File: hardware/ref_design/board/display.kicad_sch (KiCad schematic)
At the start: 29 parts, among them J3 FH12-50S-0.5SH(55), Q5 AO3400A, Q6 AO3400A, U6 MCP6002

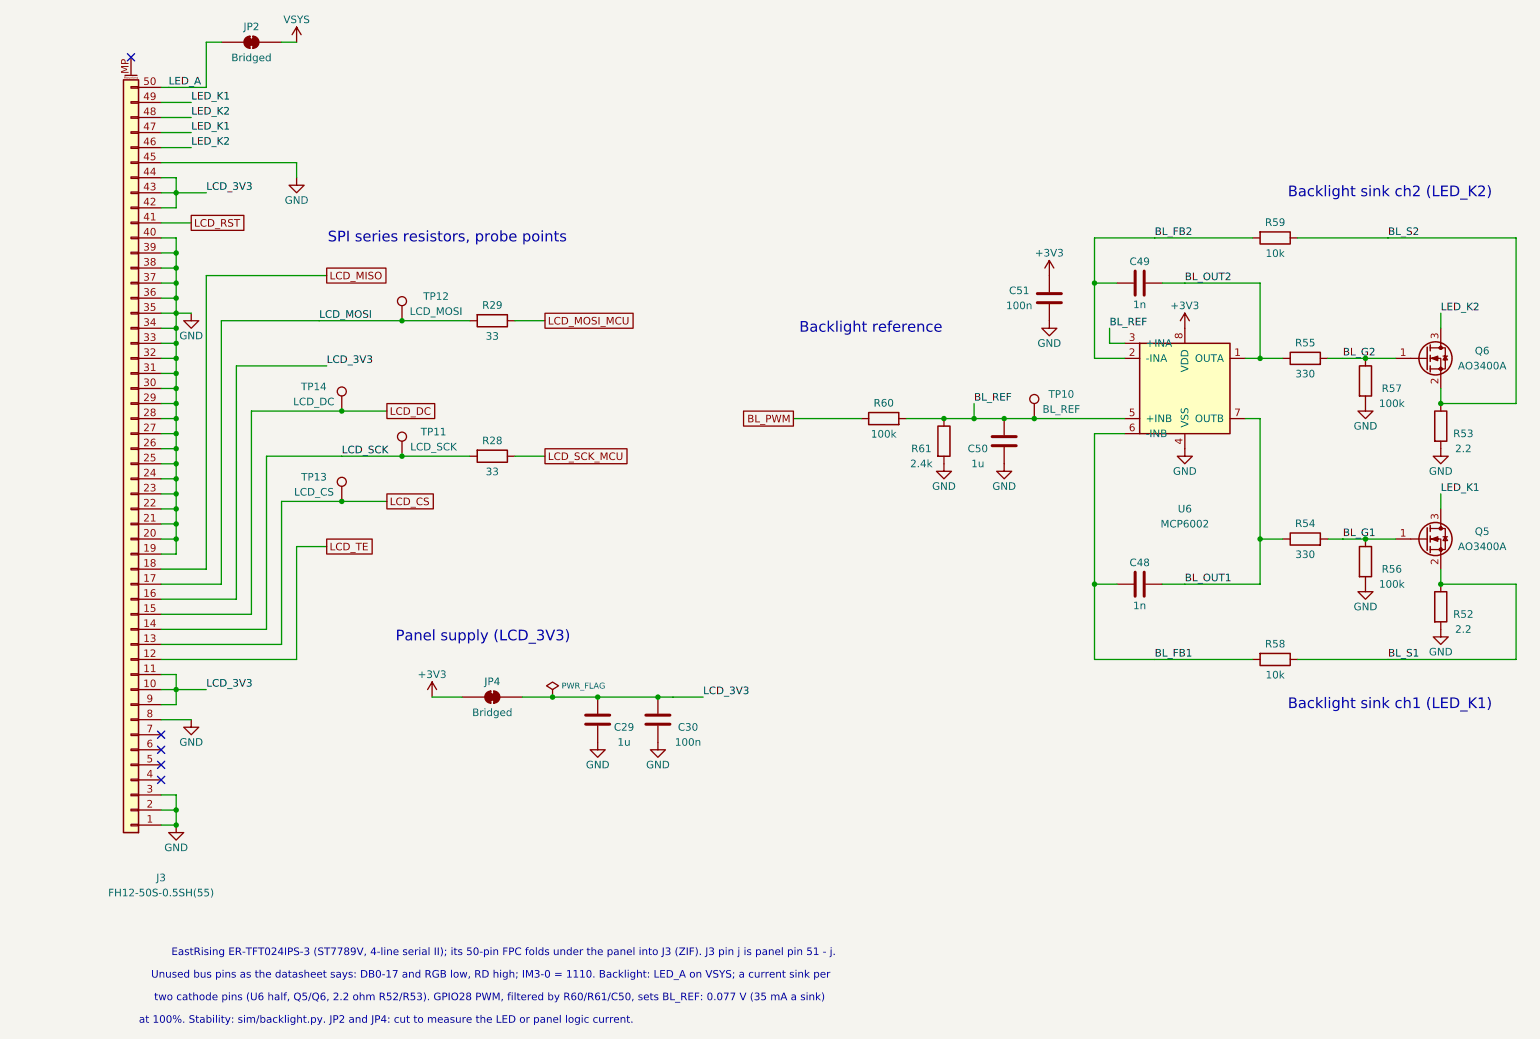
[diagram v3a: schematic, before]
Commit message: ref_design: schematic regenerated for the ER-TFT035IPS-6 (ERC 0, netlist and pin review pass)
Co-Authored-By: Claude Sonnet 5.5 <noreply@anthropic.com>
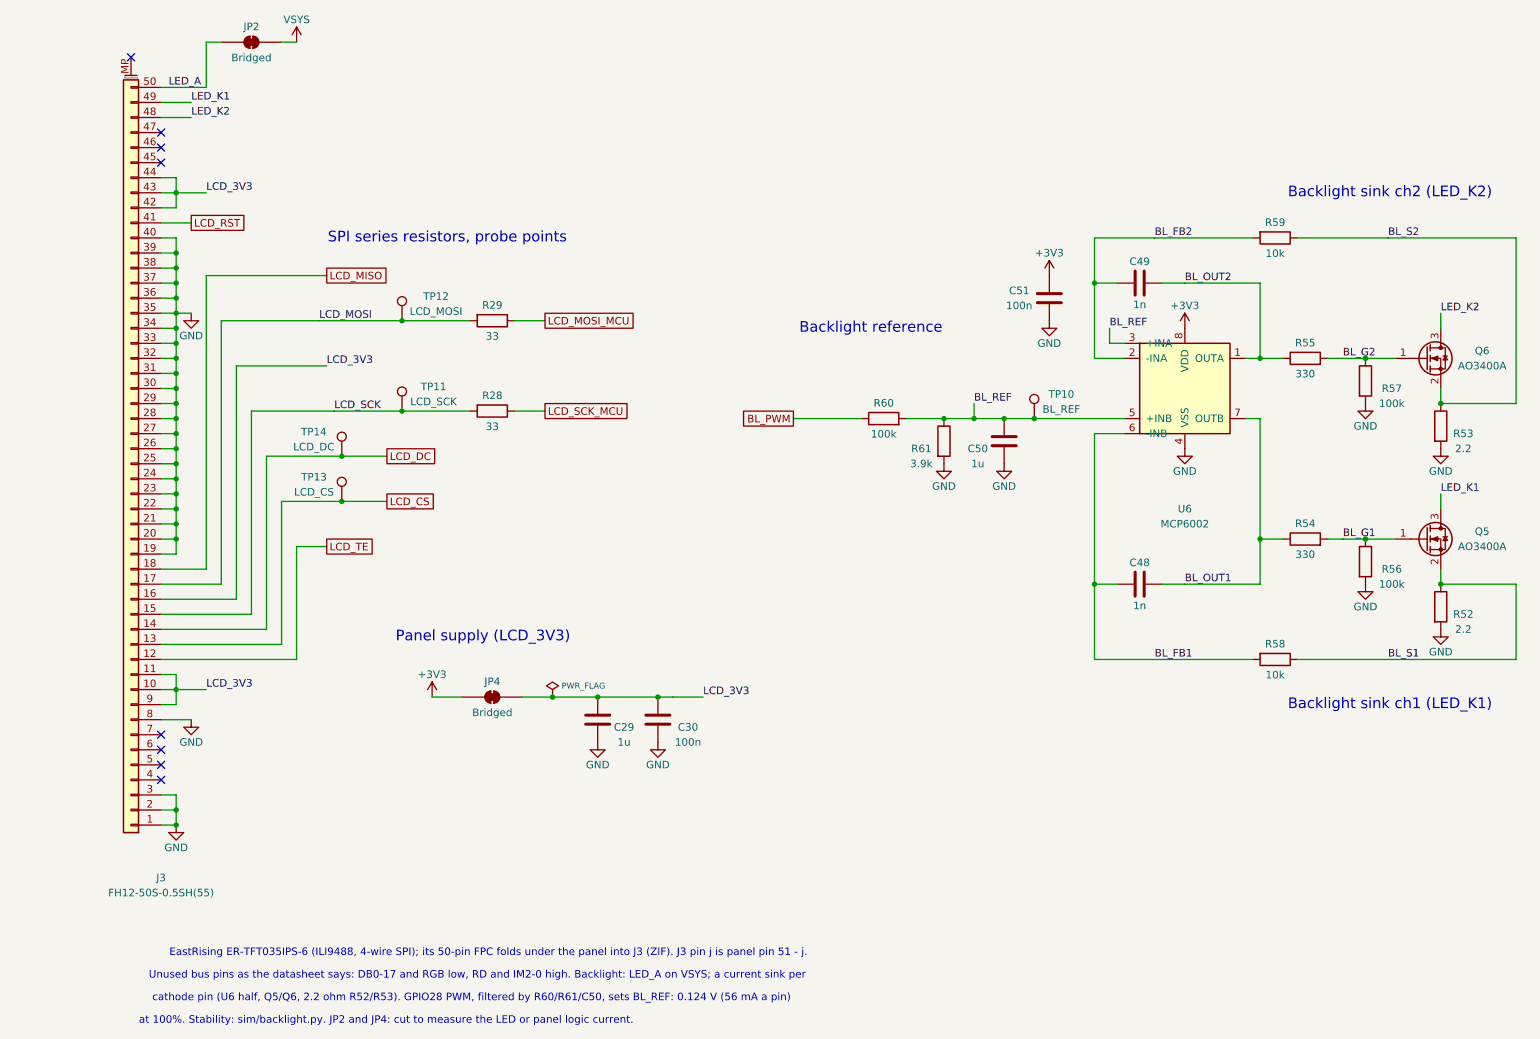
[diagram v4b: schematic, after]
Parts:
- R61: value 2.4k -> 3.9k; LCSC C25882 -> C51721; MPN 0402WGF2401TCE -> 0402WGF3901TCE
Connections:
- net GND: no longer J3.45 (Pin_45)
- net LCD_DC: now also J3.14 (Pin_14); no longer J3.15 (Pin_15)
- net LCD_SCK: now also J3.15 (Pin_15); no longer J3.14 (Pin_14)
- net LED_K1: no longer J3.47 (Pin_47)
- net LED_K2: no longer J3.46 (Pin_46)
- no-connect marks 5 -> 8
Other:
- note added: "EastRising ER-TFT035IPS-6 (ILI9488, 4-wire SPI); its 50-pin FPC folds under the panel into J3 (ZIF). J3 pin j is panel pin 51 - j."
- note added: "Unused bus pins as the datasheet says: DB0-17 and RGB low, RD and IM2-0 high. Backlight: LED_A on VSYS; a current sink per"
- note added: "cathode pin (U6 half, Q5/Q6, 2.2 ohm R52/R53). GPIO28 PWM, filtered by R60/R61/C50, sets BL_REF: 0.124 V (56 mA a pin)"
- note removed: "EastRising ER-TFT024IPS-3 (ST7789V, 4-line serial II); its 50-pin FPC folds under the panel into J3 (ZIF). J3 pin j is panel pin 51 - j."
- note removed: "Unused bus pins as the datasheet says: DB0-17 and RGB low, RD high; IM3-0 = 1110. Backlight: LED_A on VSYS; a current sink per"
- note removed: "two cathode pins (U6 half, Q5/Q6, 2.2 ohm R52/R53). GPIO28 PWM, filtered by R60/R61/C50, sets BL_REF: 0.077 V (35 mA a sink)"
- moved on the sheet: R28, TP11, TP14

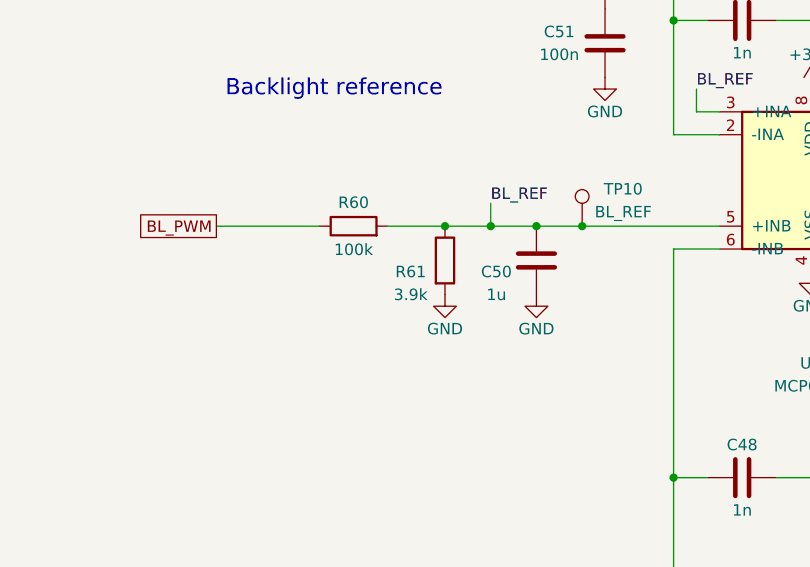
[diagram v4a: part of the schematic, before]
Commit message: ref_design V&V round 3, schematic: R61 3.74k (DEC-31), R14 47k and R43 220k with no clamp (DEC-17), RN1-RN4 47k (DEC-24), U10 buffer on VBAT_SENSE, 10k B4460 NTC for TH1, J4 JST SH, pin reviews
Co-Authored-By: Claude Sonnet 5.5 <noreply@anthropic.com>
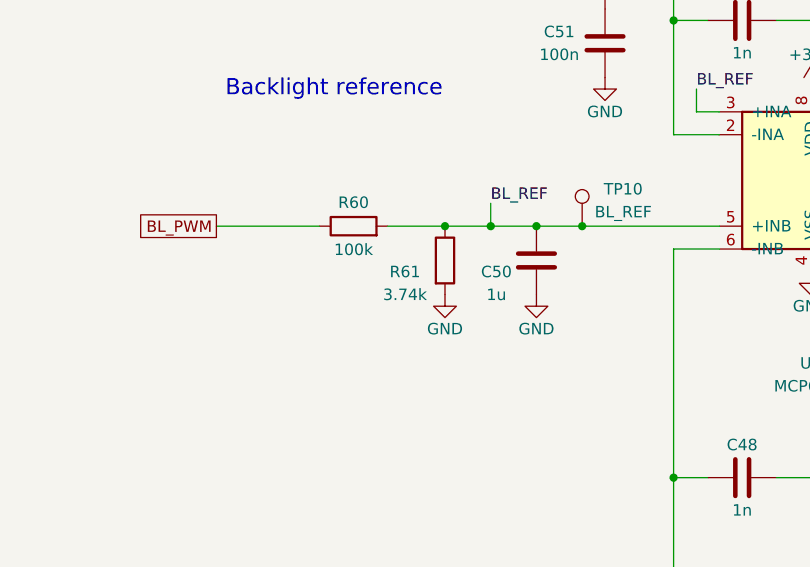
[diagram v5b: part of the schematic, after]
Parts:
- R61: value 3.9k -> 3.74k; LCSC C51721 -> C15172; MPN 0402WGF3901TCE -> 0402WGF3741TCE
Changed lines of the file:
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@@
 		(dnp no)
 		(property "Reference" "R61"
-			(at 156.21 90.17 0)
-			(show_name no)
-			(do_not_autoplace no)
-			(effects
-				(font
-					(size 1.27 1.27)
-				)
-			)
-		)
-		(property "Value" "3.9k"
-			(at 156.21 92.71 0)
+			(at 155.575 90.17 0)
+			(show_name no)
+			(do_not_autoplace no)
+			(effects
+				(font
+					(size 1.27 1.27)
+				)
+			)
+		)
+		(property "Value" "3.74k"
+			(at 155.575 92.71 0)
 			(show_name no)
 			(do_not_autoplace no)
@@
 			)
 		)
-		(property "LCSC" "C51721"
+		(property "LCSC" "C15172"
 			(at 160.02 88.9 0)
 			(hide yes)
@@
 			)
 		)
-		(property "MPN" "0402WGF3901TCE"
+		(property "MPN" "0402WGF3741TCE"
 			(at 160.02 88.9 0)
 			(hide yes)
@@
 		(in_pos_files yes)
 		(dnp no)
-		(property "Reference" "#PWR076"
+		(property "Reference" "#PWR080"
 			(at 50.8 21.59 0)
 			(hide yes)
@@
 			(project "battler"
 				(path "/8922e0a8-6f76-52f6-b0ec-4de6a784796f/99b2b9c1-5178-5fd9-a3fe-39987bd8b040"
-					(reference "#PWR076")
+					(reference "#PWR080")
 					(unit 1)
 				)
@@
 		(in_pos_files yes)
 		(dnp no)
-		(property "Reference" "#PWR077"
+		(property "Reference" "#PWR081"
 			(at 33.02 67.31 0)
 			(hide yes)
@@
 			(project "battler"
 				(path "/8922e0a8-6f76-52f6-b0ec-4de6a784796f/99b2b9c1-5178-5fd9-a3fe-39987bd8b040"
-					(reference "#PWR077")
+					(reference "#PWR081")
 					(unit 1)
 				)
@@
 		(in_pos_files yes)
 		(dnp no)
-		(property "Reference" "#PWR078"
+		(property "Reference" "#PWR082"
 			(at 33.02 135.89 0)
 			(hide yes)
@@
 			(project "battler"
 				(path "/8922e0a8-6f76-52f6-b0ec-4de6a784796f/99b2b9c1-5178-5fd9-a3fe-39987bd8b040"
-					(reference "#PWR078")
+					(reference "#PWR082")
 					(unit 1)
 				)
@@
 		(in_pos_files yes)
 		(dnp no)
-		(property "Reference" "#PWR079"
+		(property "Reference" "#PWR083"
 			(at 30.48 153.67 0)
 			(hide yes)
@@
 			(project "battler"
 				(path "/8922e0a8-6f76-52f6-b0ec-4de6a784796f/99b2b9c1-5178-5fd9-a3fe-39987bd8b040"
-					(reference "#PWR079")
+					(reference "#PWR083")
 					(unit 1)
 				)
@@
 		(in_pos_files yes)
 		(dnp no)
-		(property "Reference" "#PWR080"
+		(property "Reference" "#PWR084"
 			(at 73.66 132.08 0)
 			(hide yes)
@@
 			(project "battler"
 				(path "/8922e0a8-6f76-52f6-b0ec-4de6a784796f/99b2b9c1-5178-5fd9-a3fe-39987bd8b040"
-					(reference "#PWR080")
+					(reference "#PWR084")
 					(unit 1)
 				)
@@
 		(in_pos_files yes)
 		(dnp no)
-		(property "Reference" "#PWR081"
+		(property "Reference" "#PWR085"
 			(at 101.6 139.7 0)
 			(hide yes)
@@
 			(project "battler"
 				(path "/8922e0a8-6f76-52f6-b0ec-4de6a784796f/99b2b9c1-5178-5fd9-a3fe-39987bd8b040"
-					(reference "#PWR081")
+					(reference "#PWR085")
 					(unit 1)
 				)
@@
 		(in_pos_files yes)
 		(dnp no)
-		(property "Reference" "#PWR082"
+		(property "Reference" "#PWR086"
 			(at 111.76 139.7 0)
 			(hide yes)
@@
 			(project "battler"
 				(path "/8922e0a8-6f76-52f6-b0ec-4de6a784796f/99b2b9c1-5178-5fd9-a3fe-39987bd8b040"
-					(reference "#PWR082")
+					(reference "#PWR086")
 					(unit 1)
 				)
@@
 		(in_pos_files yes)
 		(dnp no)
-		(property "Reference" "#PWR083"
+		(property "Reference" "#PWR087"
 			(at 160.02 92.71 0)
 			(hide yes)
@@
 			(project "battler"
 				(path "/8922e0a8-6f76-52f6-b0ec-4de6a784796f/99b2b9c1-5178-5fd9-a3fe-39987bd8b040"
-					(reference "#PWR083")
+					(reference "#PWR087")
 					(unit 1)
 				)
@@
 		(in_pos_files yes)
 		(dnp no)
-		(property "Reference" "#PWR084"
+		(property "Reference" "#PWR088"
 			(at 170.18 92.71 0)
 			(hide yes)
@@
 			(project "battler"
 				(path "/8922e0a8-6f76-52f6-b0ec-4de6a784796f/99b2b9c1-5178-5fd9-a3fe-39987bd8b040"
-					(reference "#PWR084")
+					(reference "#PWR088")
 					(unit 1)
 				)
@@
 		(in_pos_files yes)
 		(dnp no)
-		(property "Reference" "#PWR085"
+		(property "Reference" "#PWR089"
 			(at 177.8 60.96 0)
 			(hide yes)
@@
 			(project "battler"
 				(path "/8922e0a8-6f76-52f6-b0ec-4de6a784796f/99b2b9c1-5178-5fd9-a3fe-39987bd8b040"
-					(reference "#PWR085")
+					(reference "#PWR089")
 					(unit 1)
 				)
@@
 		(in_pos_files yes)
 		(dnp no)
-		(property "Reference" "#PWR086"
+		(property "Reference" "#PWR090"
 			(at 177.8 68.58 0)
 			(hide yes)
@@
 			(project "battler"
 				(path "/8922e0a8-6f76-52f6-b0ec-4de6a784796f/99b2b9c1-5178-5fd9-a3fe-39987bd8b040"
-					(reference "#PWR086")
+					(reference "#PWR090")
 					(unit 1)
 				)
@@
 		(in_pos_files yes)
 		(dnp no)
-		(property "Reference" "#PWR087"
+		(property "Reference" "#PWR091"
 			(at 200.66 69.85 0)
 			(hide yes)
@@
 			(project "battler"
 				(path "/8922e0a8-6f76-52f6-b0ec-4de6a784796f/99b2b9c1-5178-5fd9-a3fe-39987bd8b040"
-					(reference "#PWR087")
+					(reference "#PWR091")
 					(unit 1)
 				)
@@
 		(in_pos_files yes)
 		(dnp no)
-		(property "Reference" "#PWR088"
+		(property "Reference" "#PWR092"
 			(at 200.66 90.17 0)
 			(hide yes)
@@
 			(project "battler"
 				(path "/8922e0a8-6f76-52f6-b0ec-4de6a784796f/99b2b9c1-5178-5fd9-a3fe-39987bd8b040"
-					(reference "#PWR088")
+					(reference "#PWR092")
 					(unit 1)
 				)
@@
 		(in_pos_files yes)
 		(dnp no)
-		(property "Reference" "#PWR089"
+		(property "Reference" "#PWR093"
 			(at 231.14 82.55 0)
 			(hide yes)
@@
 			(project "battler"
 				(path "/8922e0a8-6f76-52f6-b0ec-4de6a784796f/99b2b9c1-5178-5fd9-a3fe-39987bd8b040"
-					(reference "#PWR089")
+					(reference "#PWR093")
 					(unit 1)
 				)
@@
 		(in_pos_files yes)
 		(dnp no)
-		(property "Reference" "#PWR090"
+		(property "Reference" "#PWR094"
 			(at 243.84 90.17 0)
 			(hide yes)
@@
 			(project "battler"
 				(path "/8922e0a8-6f76-52f6-b0ec-4de6a784796f/99b2b9c1-5178-5fd9-a3fe-39987bd8b040"
-					(reference "#PWR090")
+					(reference "#PWR094")
 					(unit 1)
 				)
@@
 		(in_pos_files yes)
 		(dnp no)
-		(property "Reference" "#PWR091"
+		(property "Reference" "#PWR095"
 			(at 231.14 113.03 0)
 			(hide yes)
@@
 			(project "battler"
 				(path "/8922e0a8-6f76-52f6-b0ec-4de6a784796f/99b2b9c1-5178-5fd9-a3fe-39987bd8b040"
-					(reference "#PWR091")
+					(reference "#PWR095")
 					(unit 1)
 				)
@@
 		(in_pos_files yes)
 		(dnp no)
-		(property "Reference" "#PWR092"
+		(property "Reference" "#PWR096"
 			(at 243.84 120.65 0)
 			(hide yes)
@@
 			(project "battler"
 				(path "/8922e0a8-6f76-52f6-b0ec-4de6a784796f/99b2b9c1-5178-5fd9-a3fe-39987bd8b040"
-					(reference "#PWR092")
-					(unit 1)
-				)
+					(reference "#PWR096")
+					(unit 1)
+				)
